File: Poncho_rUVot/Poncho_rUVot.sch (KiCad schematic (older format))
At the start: 20 parts, among them J1 Screw_Terminal_01x03, K1 SANYOU_SRD_Form_C, P1 Conn_01x03, P2 Conn_01x03, P3 Conn_01x04, P4 Conn_01x03, P5 Conn_01x02, P6 Conn_01x02, P7 Conn_01x06, P8 Conn_01x04, P9 Conn_01x08, Q1 BC548, Q2 BC548

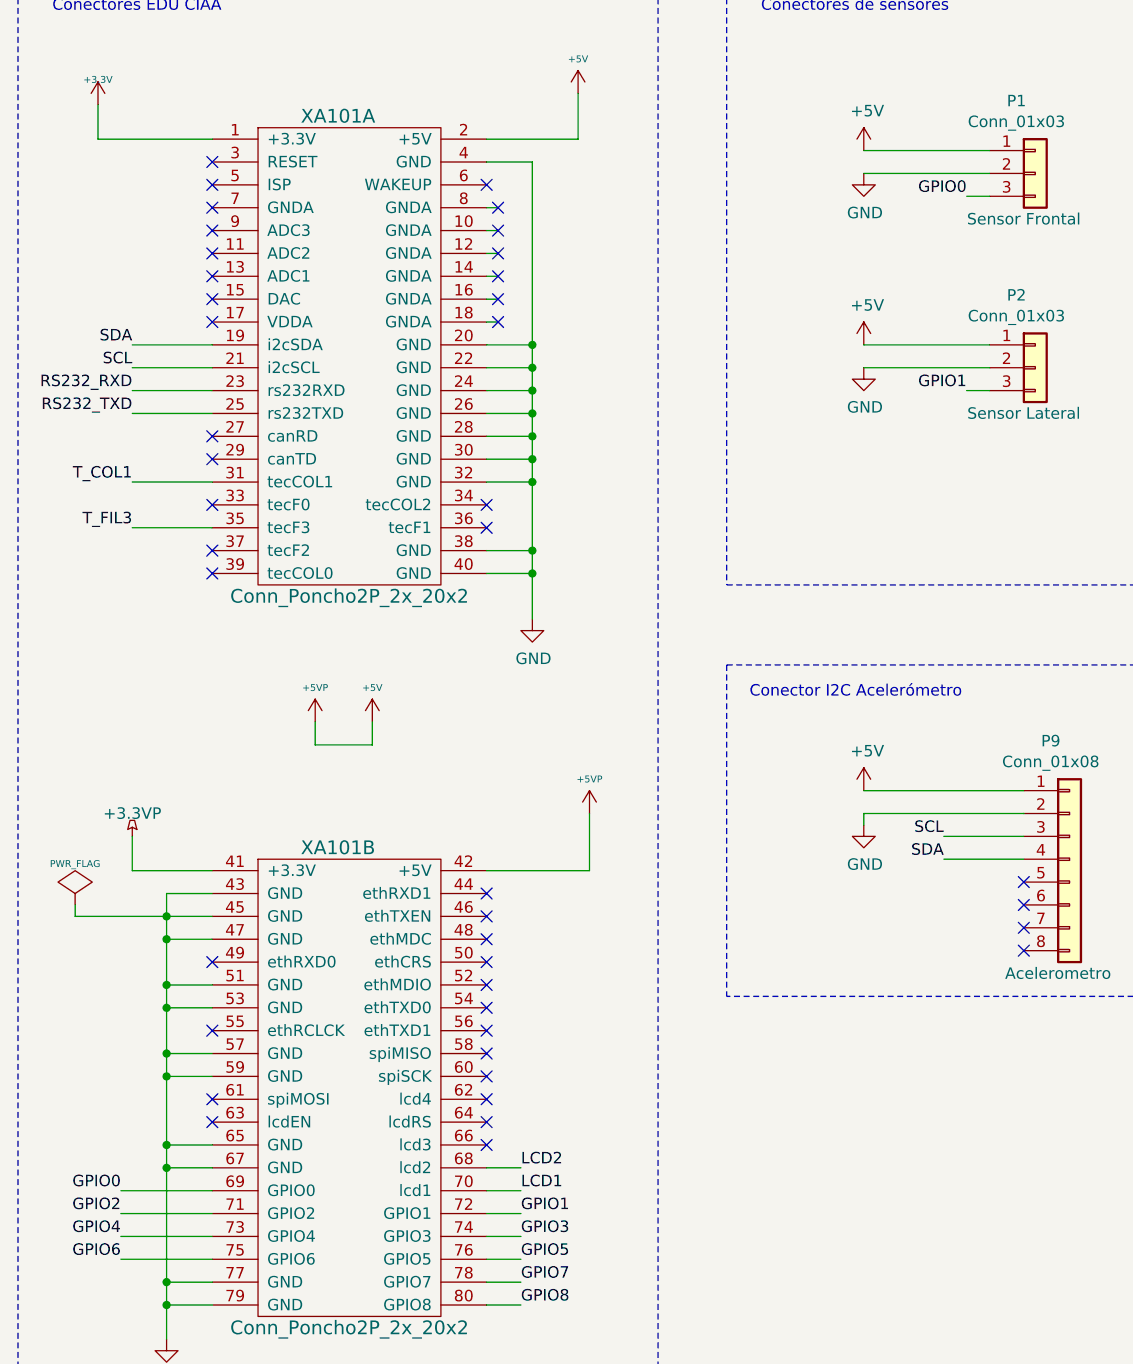
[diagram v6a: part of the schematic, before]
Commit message: Se elimina un puente
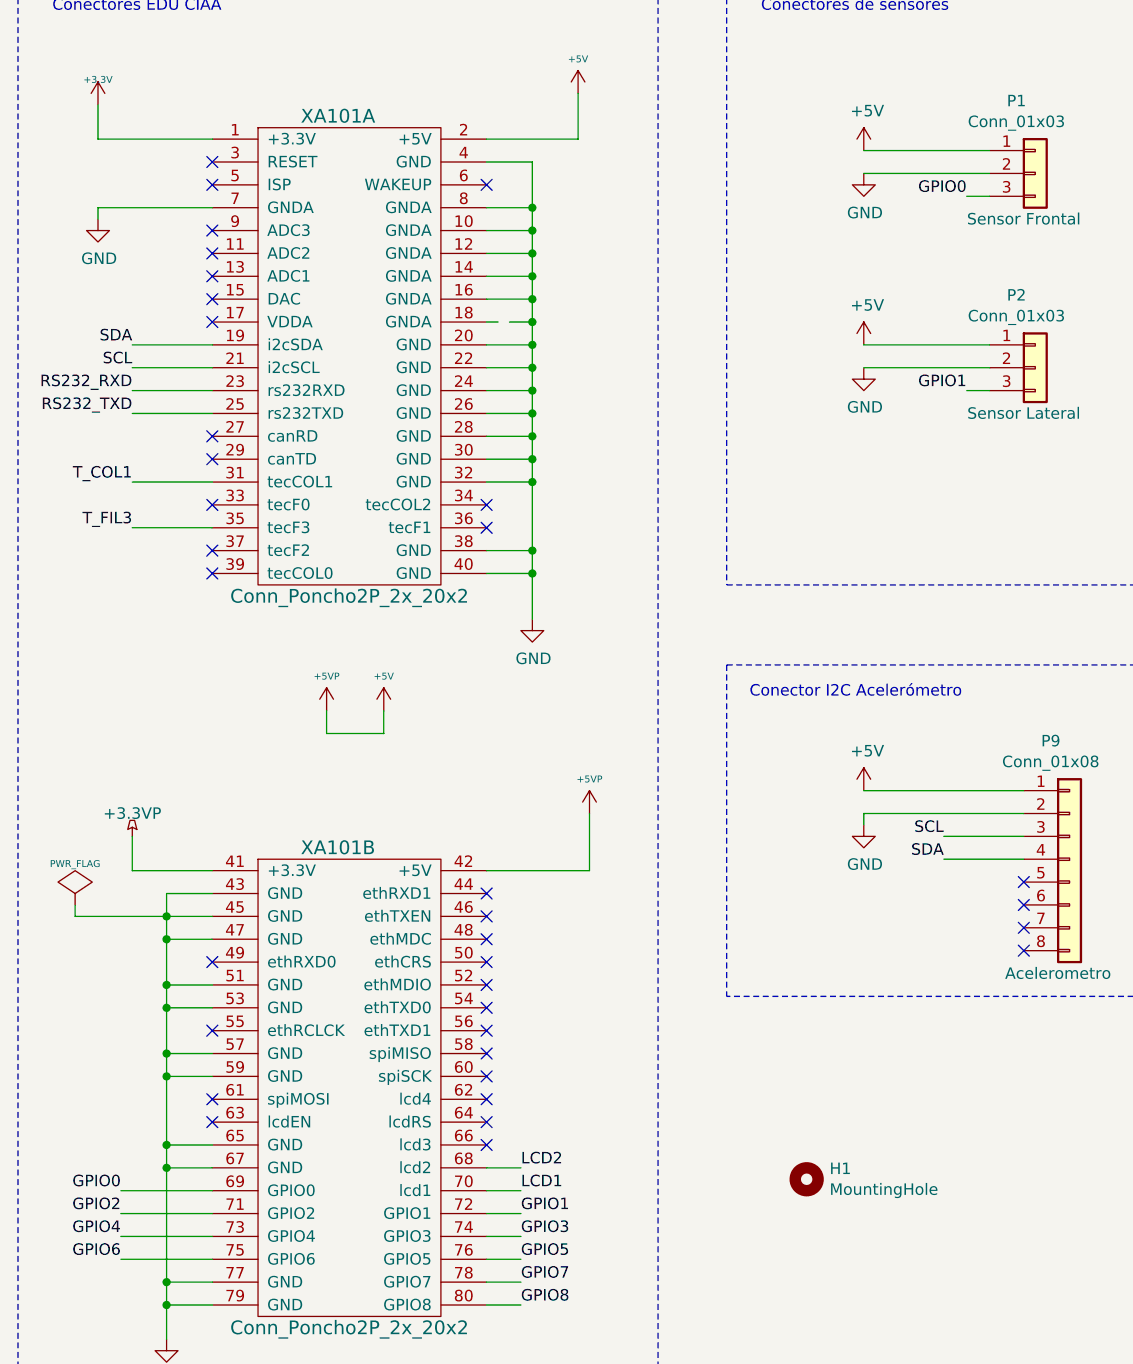
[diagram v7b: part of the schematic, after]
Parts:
- added H1: MountingHole, MountingHole:MountingHole_2.5mm, symbol Mechanical:MountingHole
- Q1, Q2: footprint Package_TO_SOT_THT:TO-92L -> Package_TO_SOT_THT:TO-92L_Wide
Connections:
- net GND: now also XA101.10 (GNDA), XA101.12 (GNDA), XA101.14 (GNDA), XA101.16 (GNDA), XA101.7 (GNDA), XA101.8 (GNDA)
- no-connect marks 44 -> 37
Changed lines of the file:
@@
 $EndComp
 Wire Wire Line
-	3000 1550 3000 2350
+	3000 1550 3000 1750
 Wire Wire Line
 	3000 3250 2800 3250
@@
 $EndComp
 Wire Wire Line
-	2800 1750 2850 1750
-Wire Wire Line
 	2850 2250 2800 2250
 Wire Wire Line
-	2800 2150 2850 2150
-Wire Wire Line
-	2800 2050 2850 2050
-Wire Wire Line
-	2800 1950 2850 1950
-Wire Wire Line
-	2800 1850 2850 1850
-Wire Wire Line
 	1600 4650 1250 4650
 Wire Wire Line
 	1250 4650 1250 4500
-Wire Wire Line
-	2800 4650 3250 4650
 Wire Wire Line
 	3250 4650 3250 4400
@@
 F 0 "Q2" H 10541 5596 50  0000 L CNN
 F 1 "BC548" H 10541 5505 50  0000 L CNN
-F 2 "Package_TO_SOT_THT:TO-92L" H 10550 5475 50  0001 L CIN
+F 2 "Package_TO_SOT_THT:TO-92L_Wide" H 10550 5475 50  0001 L CIN
 F 3 "https://www.onsemi.com/pub/Collateral/BC550-D.pdf" H 10350 5550 50  0001 L CNN
 	1    10350 5550
@@
 F 0 "Q1" H 7741 5596 50  0000 L CNN
 F 1 "BC548" H 7741 5505 50  0000 L CNN
-F 2 "Package_TO_SOT_THT:TO-92L" H 7750 5475 50  0001 L CIN
+F 2 "Package_TO_SOT_THT:TO-92L_Wide" H 7750 5475 50  0001 L CIN
 F 3 "https://www.onsemi.com/pub/Collateral/BC550-D.pdf" H 7550 5550 50  0001 L CNN
 	1    7550 5550
@@
 	1    0    0    -1
 $EndComp
-NoConn ~ 1600 1750
-NoConn ~ 2850 1750
-NoConn ~ 2850 1850
-NoConn ~ 2850 1950
-NoConn ~ 2850 2050
-NoConn ~ 2850 2150
-NoConn ~ 2850 2250
 $Comp
 L Relay:SANYOU_SRD_Form_C K1
@@
 $EndBitmap
 $Comp
-L Poncho_rUVot-rescue:+5V #PWR0118
-U 1 1 6080CF4B
-P 2300 4000
-F 0 "#PWR0118" H 2300 4090 20  0001 C CNN
-F 1 "+5V" H 2300 4150 30  0000 C CNN
-F 2 "" H 2300 4000 60  0000 C CNN
-F 3 "" H 2300 4000 60  0000 C CNN
-	1    2300 4000
-	1    0    0    -1
-$EndComp
-$Comp
-L Poncho_rUVot-rescue:+5VP #PWR0119
-U 1 1 608141D3
-P 2050 4000
-F 0 "#PWR0119" H 2050 4090 20  0001 C CNN
-F 1 "+5VP" H 2050 4150 30  0000 C CNN
-F 2 "" H 2050 4000 60  0000 C CNN
-F 3 "" H 2050 4000 60  0000 C CNN
-	1    2050 4000
-	1    0    0    -1
-$EndComp
-Wire Wire Line
-	2050 4000 2050 4100
-Wire Wire Line
-	2050 4100 2300 4100
-Wire Wire Line
-	2300 4100 2300 4000
-$Comp
 L Poncho_rUVot-rescue:Screw_Terminal_01x03-Connector-conectores-rescue J1
 U 1 1 606412BA
@@
 	1    0    0    -1
 $EndComp
+$Comp
+L Mechanical:MountingHole H1
+U 1 1 608D861A
+P 4200 6000
+F 0 "H1" H 4300 6046 50  0000 L CNN
+F 1 "MountingHole" H 4300 5955 50  0000 L CNN
+F 2 "MountingHole:MountingHole_2.5mm" H 4200 6000 50  0001 C CNN
+F 3 "~" H 4200 6000 50  0001 C CNN
+	1    4200 6000
+	1    0    0    -1
+$EndComp
+Wire Wire Line
+	2800 4650 3250 4650
+Wire Wire Line
+	1100 1750 1100 1800
+Wire Wire Line
+	1100 1750 1600 1750
+$Comp
+L Poncho_rUVot-rescue:+5V #PWR0118
+U 1 1 6080CF4B
+P 2350 3950
+F 0 "#PWR0118" H 2350 4040 20  0001 C CNN
+F 1 "+5V" H 2350 4100 30  0000 C CNN
+F 2 "" H 2350 3950 60  0000 C CNN
+F 3 "" H 2350 3950 60  0000 C CNN
+	1    2350 3950
+	1    0    0    -1
+$EndComp
+$Comp
+L Poncho_rUVot-rescue:+5VP #PWR0119
+U 1 1 608141D3
+P 2100 3950
+F 0 "#PWR0119" H 2100 4040 20  0001 C CNN
+F 1 "+5VP" H 2100 4100 30  0000 C CNN
+F 2 "" H 2100 3950 60  0000 C CNN
+F 3 "" H 2100 3950 60  0000 C CNN
+	1    2100 3950
+	1    0    0    -1
+$EndComp
+Wire Wire Line
+	2100 3950 2100 4050
+Wire Wire Line
+	2100 4050 2350 4050
+Wire Wire Line
+	2350 4050 2350 3950
+Wire Wire Line
+	2800 1750 3000 1750
+Connection ~ 3000 1750
+Wire Wire Line
+	3000 1750 3000 1850
+Wire Wire Line
+	2800 1850 3000 1850
+Connection ~ 3000 1850
+Wire Wire Line
+	3000 1850 3000 1950
+Wire Wire Line
+	2800 1950 3000 1950
+Connection ~ 3000 1950
+Wire Wire Line
+	3000 1950 3000 2050
+Wire Wire Line
+	2800 2050 3000 2050
+Connection ~ 3000 2050
+Wire Wire Line
+	3000 2050 3000 2150
+Wire Wire Line
+	2800 2150 3000 2150
+Connection ~ 3000 2150
+Wire Wire Line
+	3000 2150 3000 2250
+Wire Wire Line
+	2900 2250 3000 2250
+Connection ~ 3000 2250
+Wire Wire Line
+	3000 2250 3000 2350
+$Comp
+L Poncho_rUVot-rescue:GND #PWR?
+U 1 1 608D6CD1
+P 1100 1800
+F 0 "#PWR?" H 1100 1550 50  0001 C CNN
+F 1 "GND" H 1105 1627 50  0000 C CNN
+F 2 "" H 1100 1800 50  0000 C CNN
+F 3 "" H 1100 1800 50  0000 C CNN
+	1    1100 1800
+	1    0    0    -1
+$EndComp

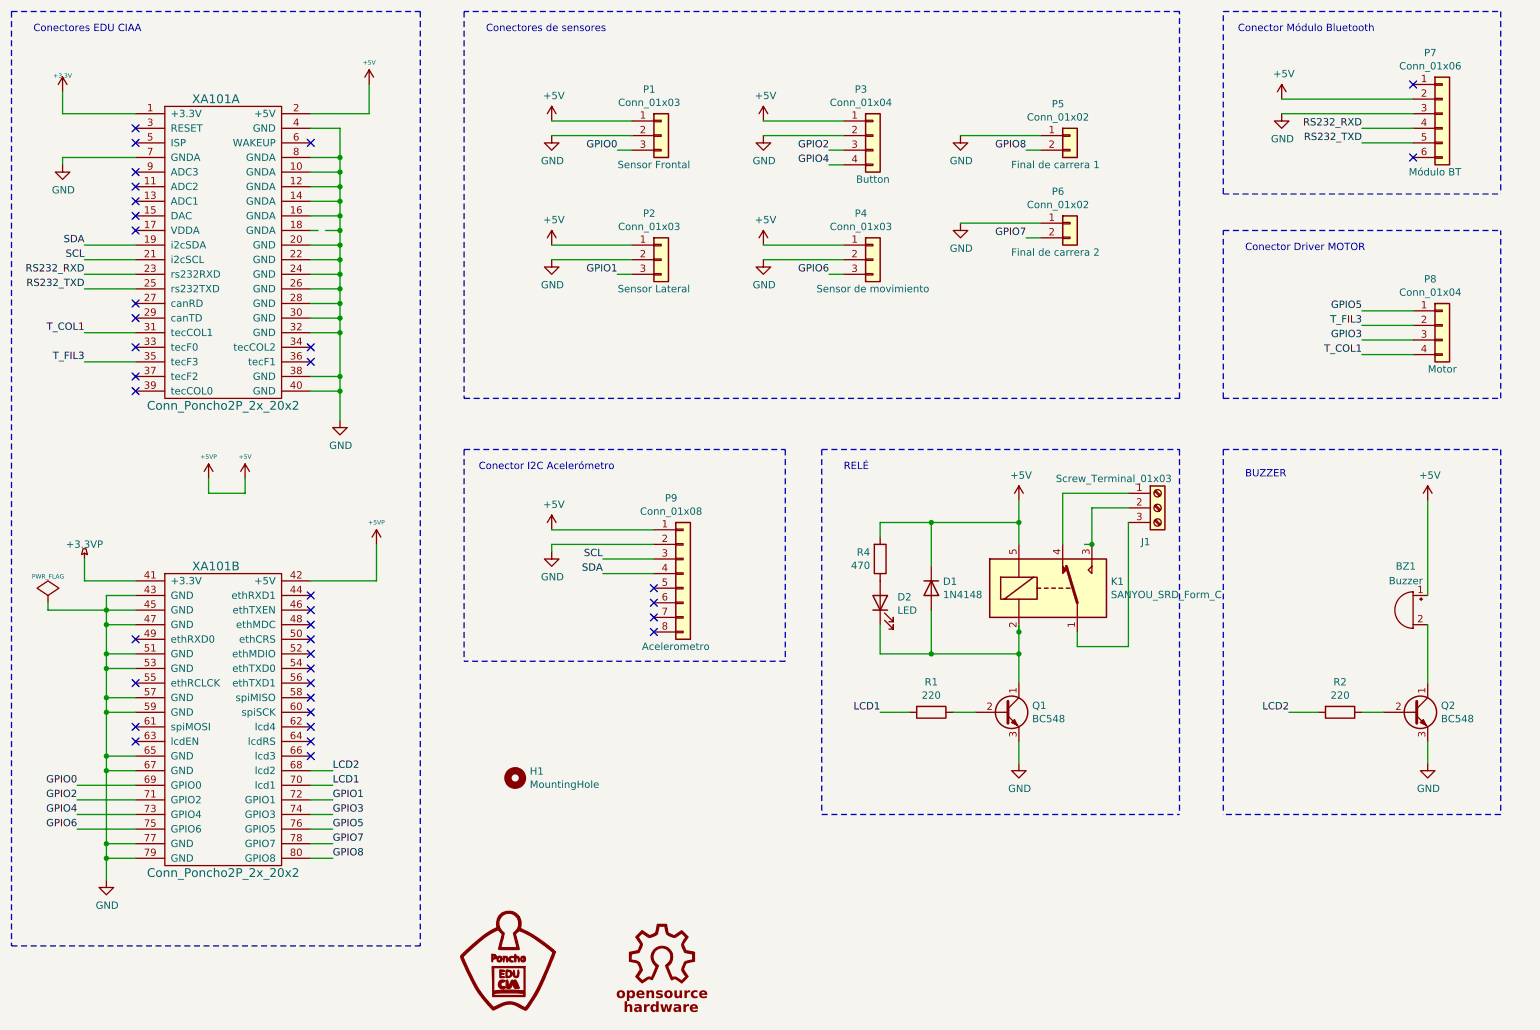
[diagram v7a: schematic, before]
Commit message: se agrega led testigo
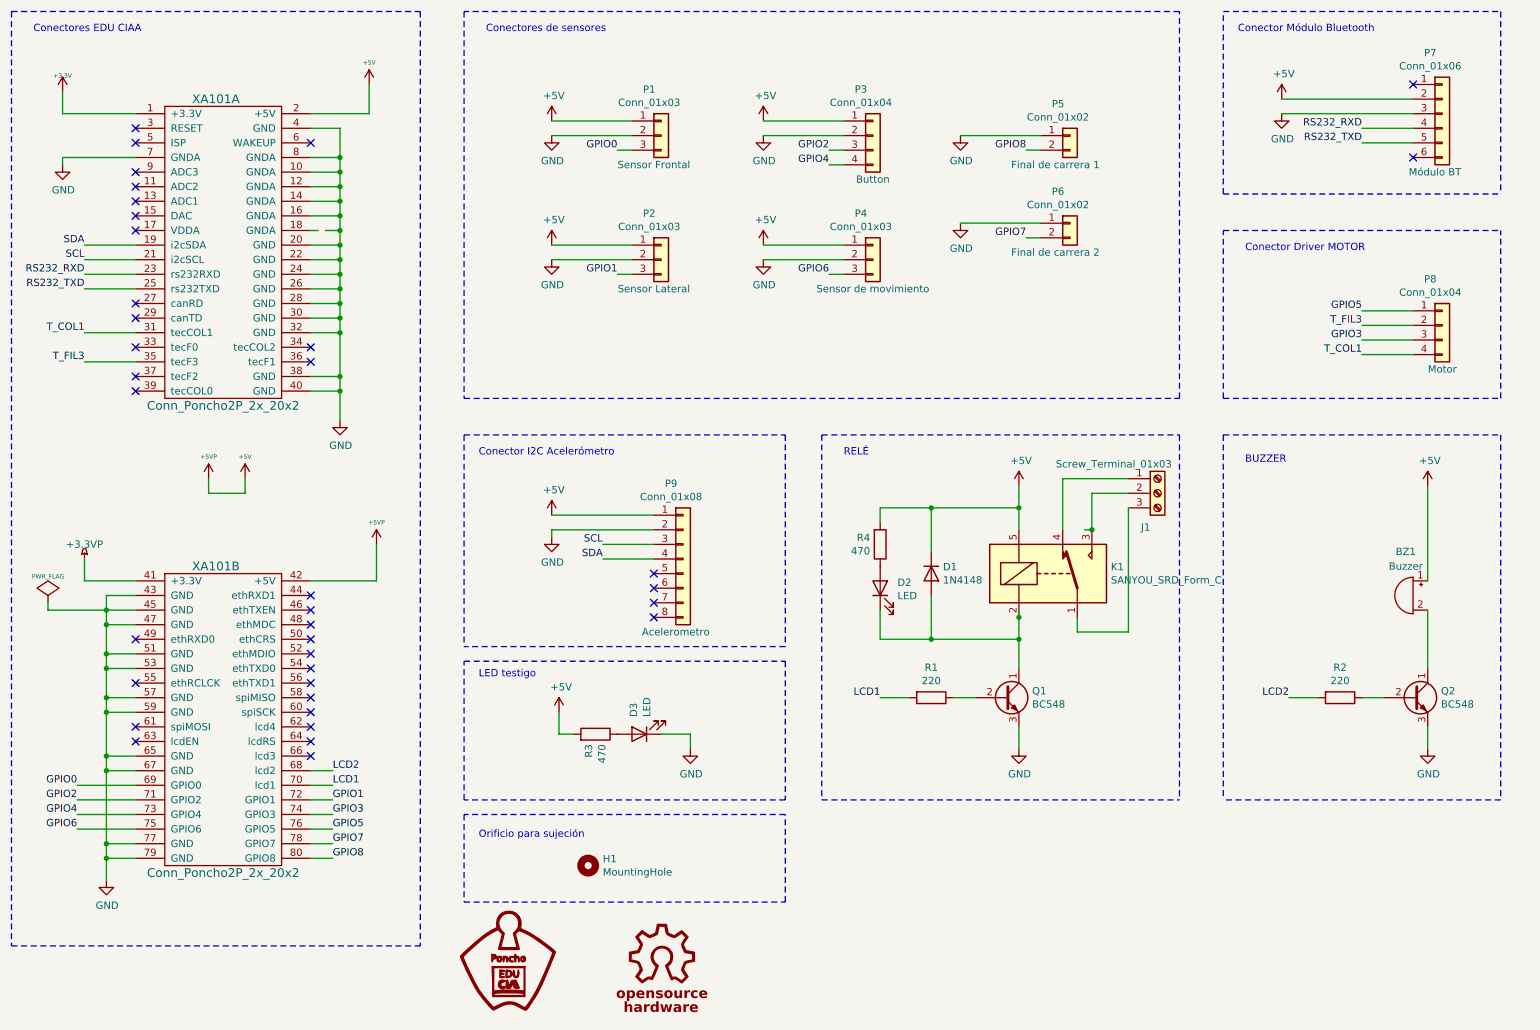
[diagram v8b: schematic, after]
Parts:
- added D3: LED, LED_THT:LED_D5.0mm, symbol Poncho_rUVot-rescue:LED-Device-conectores-rescue
- added R3: 470, Resistor_THT:R_Axial_DIN0204_L3.6mm_D1.6mm_P7.62mm_Horizontal, symbol Poncho_rUVot-rescue:R-Device-conectores-rescue
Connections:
- net +5V: now also R3.2
- net GND: now also D3.1 (K)
- new net: D3.2 (A), R3.1
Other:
- note added: "LED testigo\n\n"
- note added: "Orificio para sujeción\n\n"
- moved on the sheet: BZ1, D1, D2, H1, J1, K1, P9, Q1, Q2, R1, R2, R4
